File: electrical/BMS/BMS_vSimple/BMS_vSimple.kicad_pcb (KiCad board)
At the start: 2 copper layers, 127 parts, among them J1 Conn_01x04_Pin, J2 Conn_02x12_Top_Bottom, J3 Conn_01x13_Socket, Q6 BCP56, U1 STM32F412RGTx, U2 BQ79652PAPRQ1, U3 ISO1044BD, U4 CD74HC4067M

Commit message: updated pcb
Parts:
- added C39: 100n, Capacitor_SMD:C_0603_1608Metric, F.Cu at (122.4, 81.5)
- added C40: 100n, Capacitor_SMD:C_0603_1608Metric, F.Cu at (130.7, 81.5)
- added C41: 100n, Capacitor_SMD:C_0603_1608Metric, F.Cu at (134.8, 68.7)
- added C42: 100n, Capacitor_SMD:C_0603_1608Metric, F.Cu at (122.6, 64.3)
- added C43: 100n, Capacitor_SMD:C_0603_1608Metric, F.Cu at (118.0, 73.9)
- added H1: MountingHole, MountingHole:MountingHole_2.2mm_M2, F.Cu at (34.0, 65.8)
- added H2: MountingHole, MountingHole:MountingHole_2.2mm_M2, F.Cu at (95.5, 65.5)
- added H3: MountingHole, MountingHole:MountingHole_2.2mm_M2, F.Cu at (154.0, 64.5)
- added H4: MountingHole, MountingHole:MountingHole_2.2mm_M2, F.Cu at (33.0, 139.0)
- added H5: MountingHole, MountingHole:MountingHole_2.2mm_M2, F.Cu at (96.5, 139.2)
- added H6: MountingHole, MountingHole:MountingHole_2.2mm_M2, F.Cu at (154.5, 140.0)
- added TP23: TestPoint, TestPoint:TestPoint_Pad_2.0x2.0mm, F.Cu at (135.1, 80.2)
- added TP24: TestPoint, TestPoint:TestPoint_Pad_2.0x2.0mm, F.Cu at (139.1, 80.2)
- moved C1 119.5 mm to (113.7, 112.1), turned to 90 degrees
- moved C37 110.2 mm to (140.5, 90.6), turned to -90 degrees
- moved R38 109.0 mm to (121.9, 121.0)
- moved R5 108.9 mm to (99.0, 118.8), turned to -90 degrees
- moved R39 104.0 mm to (121.1, 117.7), turned to 90 degrees
- moved C5 103.7 mm to (96.5, 116.0)
- moved R40 103.3 mm to (122.9, 117.6), turned to 90 degrees
- moved C32 102.1 mm to (113.6, 103.2), turned to -90 degrees
- moved C36 101.6 mm to (130.0, 89.8), turned to -90 degrees
- moved R20 100.6 mm to (89.7, 118.8), turned to -90 degrees
- moved C30 99.5 mm to (112.8, 95.3)
- moved C19 99.3 mm to (93.3, 116.0)
- moved C33 99.1 mm to (115.8, 98.8), turned to 90 degrees
- moved R10 95.0 mm to (92.7, 118.8), turned to -90 degrees
- moved R9 94.2 mm to (86.5, 118.8), turned to -90 degrees
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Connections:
- TP7 pad 1: Net-(U1-PA0) -> Net-(U1-PA14)
- U1 pad 1: unconnected-(U1-VBAT-Pad1) -> /VDD1
- U1 pad 13: unconnected-(U1-VDDA-Pad13) -> /VDD1
- U1 pad 14: Net-(U1-PA0) -> unconnected-(U1-PA0-Pad14)
- U1 pad 32: unconnected-(U1-VDD-Pad32) -> /VDD1
- U1 pad 33: unconnected-(U1-PB12-Pad33) -> Net-(U1-PB12)
- U1 pad 37: unconnected-(U1-PC6-Pad37) -> Net-(U1-PC6)
- U1 pad 48: unconnected-(U1-VDD-Pad48) -> /VDD1
- U1 pad 49: unconnected-(U1-PA14-Pad49) -> Net-(U1-PA14)
- U1 pad 64: unconnected-(U1-VDD-Pad64) -> /VDD1
- U3 pad 5: Net-(J1-Pin_2) -> Net-(J1-Pin_1)
- U3 pad 6: Net-(J1-Pin_3) -> Net-(J1-Pin_2)
- U3 pad 7: Net-(J1-Pin_1) -> Net-(J1-Pin_3)
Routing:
- net /BAT+: track 0.00 -> 170.0 mm
- net Net-(C29-Pad1): track 0.00 -> 154.3 mm, vias 0 -> 2
- net /TSREF: track 0.00 -> 120.1 mm, vias 0 -> 14
- net /AVDD: track 0.00 -> 108.9 mm, vias 0 -> 2
- net /VDD1: track 0.00 -> 91.7 mm
- net /CB12: track 0.00 -> 72.1 mm
- net /GPIO2: track 0.00 -> 69.5 mm, vias 0 -> 2
- net /GPIO1: track 0.00 -> 69.4 mm, vias 0 -> 2
- net /GPIO3: track 0.00 -> 69.0 mm, vias 0 -> 2
- net /VC11: track 0.00 -> 68.2 mm, vias 0 -> 3
- net /VC12: track 0.00 -> 67.3 mm, vias 0 -> 2
- net /CB11: track 0.00 -> 64.6 mm
- net /VC10: track 0.00 -> 61.9 mm, vias 0 -> 3
- net /CB10: track 0.00 -> 57.8 mm
- net /VC9: track 0.00 -> 56.9 mm, vias 0 -> 3
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- added copper zone on F.Cu, net /BAT+
- added copper zone on B.Cu, net GND
- added copper zone on F.Cu, net GND
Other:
- board outline added: 133.5 x 84.2 mm

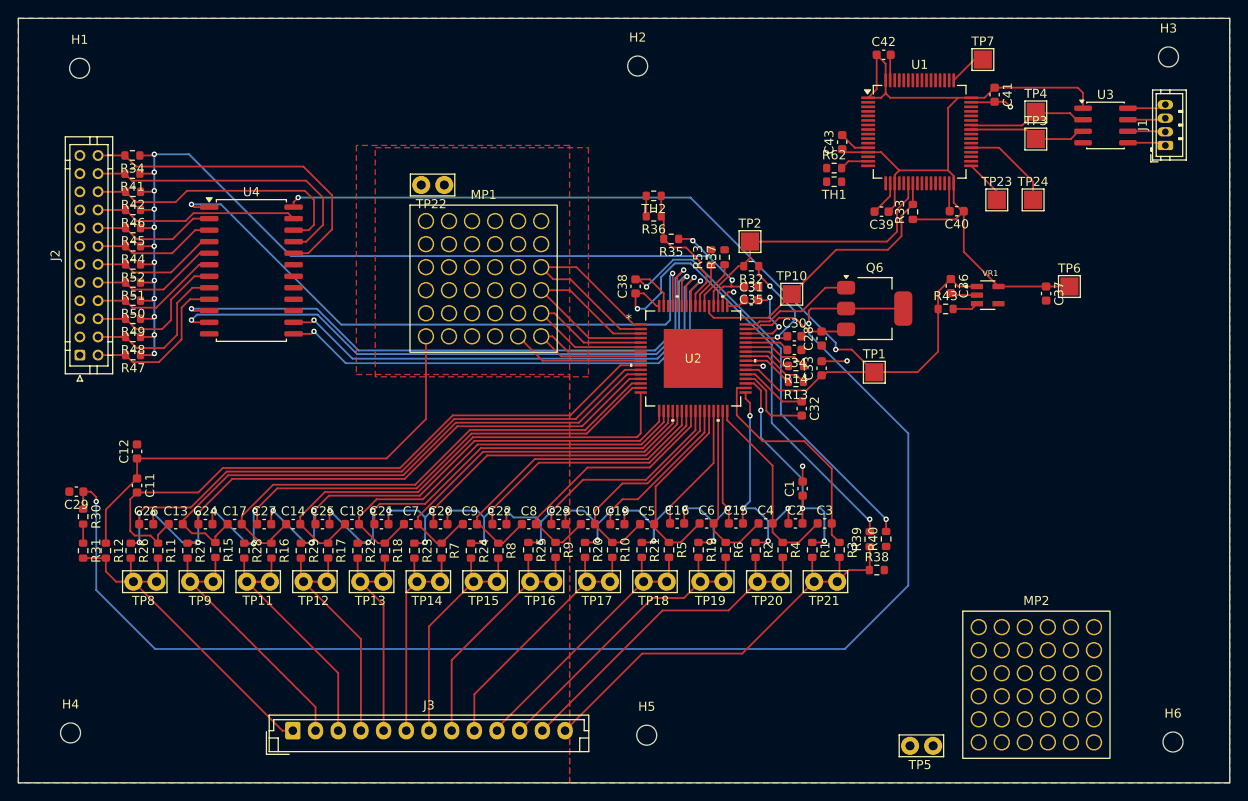
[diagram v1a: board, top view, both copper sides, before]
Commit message: adding mounting holes and finalizing dimensions
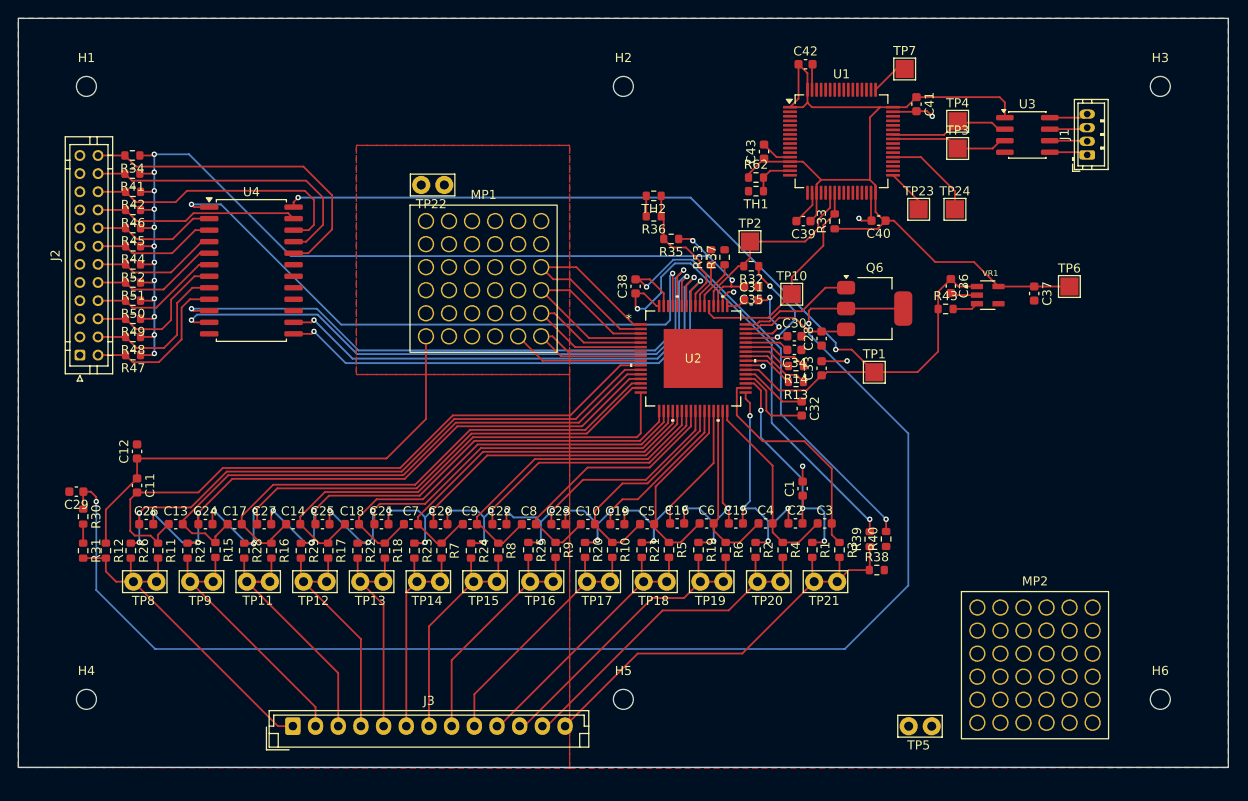
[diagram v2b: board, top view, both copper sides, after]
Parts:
- moved TP24 8.68 mm to (130.5, 81.3)
- moved C41 8.68 mm to (126.2, 69.7)
- moved C43 8.68 mm to (109.4, 74.9)
- moved R62 8.68 mm to (108.5, 77.8)
- moved TH1 8.68 mm to (108.5, 79.3)
- moved TP23 8.68 mm to (126.5, 81.3)
- moved J1 8.68 mm to (145.0, 75.3)
- moved TP7 8.68 mm to (124.9, 65.8)
- moved C39 8.68 mm to (113.8, 82.6)
- moved C40 8.68 mm to (122.1, 82.5)
- moved C42 8.68 mm to (114.0, 65.3)
- moved R33 8.68 mm to (117.2, 82.6)
- moved TP3 8.68 mm to (130.8, 74.6)
- moved TP4 8.68 mm to (130.8, 71.6)
- moved U1 8.68 mm to (118.0, 73.8)
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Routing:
- net /AFE_RX: track 31.6 -> 21.7 mm
- net /VDD1: track 91.7 -> 100.1 mm
- net /AFE_TX: track 32.6 -> 24.7 mm
- net GND: track 50.3 -> 51.8 mm, vias 7 -> 8
- net /PA1: track 3.24 -> 4.74 mm
- net /CELL_9+: track 27.0 -> 26.5 mm
- net /CELL_8+: track 25.4 -> 24.9 mm
- net /CELL_6+: track 26.4 -> 25.9 mm
- net /CELL_5+: track 28.1 -> 27.6 mm
- net /CELL_12+: track 39.8 -> 40.3 mm
- net /CELL_11+: track 30.2 -> 29.7 mm
- net /CELL_10+: track 30.5 -> 30.0 mm
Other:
- board size 133.5 x 84.2 mm -> 133.3 x 82.6 mm

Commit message: bms is smaller now...
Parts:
- added C44: 100n, Capacitor_SMD:C_0603_1608Metric, F.Cu at (127.3, 75.8)
- added C45: 4.7u, Capacitor_SMD:C_0603_1608Metric, F.Cu at (117.8, 86.8)
- added R54: 10k, Resistor_SMD:R_0603_1608Metric, F.Cu at (129.7, 76.5)
- added TP25: TestPoint, TestPoint:TestPoint_Pad_2.0x2.0mm, F.Cu at (136.8, 93.2)
- added TP26: TestPoint, TestPoint:TestPoint_Pad_2.0x2.0mm, F.Cu at (135.2, 82.2)
- J1: footprint Connector_JST:JST_ZH_B4B-ZR_1x04_P1.50mm_Vertical -> Connector_JST:JST_XH_B4B-XH-A_1x04_P2.50mm_Vertical
- J2: value Conn_02x12_Top_Bottom -> Conn_01x12; footprint Connector_JST:JST_PHD_B24B-PHDSS_2x12_P2.00mm_Vertical -> Connector_JST:JST_XH_B12B-XH-A_1x12_P2.50mm_Vertical
- J3: footprint Connector_JST:JST_EH_B13B-EH-A_1x13_P2.50mm_Vertical -> Connector_JST:JST_XH_B13B-XH-A_1x13_P2.50mm_Vertical
- moved MP2 84.3 mm to (66.5, 89.0)
- moved TP5 81.3 mm to (70.2, 78.5)
- moved H6 43.6 mm to (112.1, 120.5)
- moved H3 42.5 mm to (111.7, 77.3)
- moved J1 37.6 mm to (129.0, 109.2), turned to 0 degrees
- moved U3 25.9 mm to (133.5, 98.5), turned to -90 degrees
- moved TP7 24.7 mm to (135.2, 88.2)
- moved J3 23.9 mm to (73.0, 120.0)
- moved C42 23.2 mm to (132.8, 79.0)
- moved TP4 21.9 mm to (133.8, 93.2), turned to -90 degrees
- moved C41 21.1 mm to (131.8, 90.1), turned to 180 degrees
- moved TP3 18.7 mm to (130.8, 93.2), turned to -90 degrees
- moved R31 16.9 mm to (48.8, 110.1)
- moved TP6 16.6 mm to (127.3, 94.8), turned to 90 degrees
- moved R30 16.6 mm to (48.8, 107.1)
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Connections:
- J2 pad 1: GND -> Net-(J2-Pin_1)
- J2 pad 11: GND -> Net-(J2-Pin_11)
- J2 pad 3: GND -> Net-(J2-Pin_3)
- J2 pad 5: GND -> Net-(J2-Pin_5)
- J2 pad 7: GND -> Net-(J2-Pin_7)
- J2 pad 9: GND -> Net-(J2-Pin_9)
- R34 pad 2: Net-(J2-Pin_24) -> Net-(J2-Pin_12)
- R41 pad 2: Net-(J2-Pin_22) -> Net-(J2-Pin_11)
- R42 pad 2: Net-(J2-Pin_20) -> Net-(J2-Pin_10)
- R44 pad 2: Net-(J2-Pin_14) -> Net-(J2-Pin_7)
- R45 pad 2: Net-(J2-Pin_16) -> Net-(J2-Pin_8)
- R46 pad 2: Net-(J2-Pin_18) -> Net-(J2-Pin_9)
- R47 pad 2: Net-(J2-Pin_2) -> Net-(J2-Pin_1)
- R48 pad 2: Net-(J2-Pin_4) -> Net-(J2-Pin_2)
- R49 pad 2: Net-(J2-Pin_6) -> Net-(J2-Pin_3)
- R50 pad 2: Net-(J2-Pin_8) -> Net-(J2-Pin_4)
- R51 pad 2: Net-(J2-Pin_10) -> Net-(J2-Pin_5)
- R52 pad 2: Net-(J2-Pin_12) -> Net-(J2-Pin_6)
- TP24 pad 1: Net-(U1-PC6) -> Net-(U1-PC10)
- U1 pad 30: unconnected-(U1-VCAP_1-Pad30) -> Net-(U1-VCAP_1)
- U1 pad 37: Net-(U1-PC6) -> unconnected-(U1-PC6-Pad37)
- U1 pad 46: unconnected-(U1-PA13-Pad46) -> Net-(U1-PA13)
- U1 pad 51: unconnected-(U1-PC10-Pad51) -> Net-(U1-PC10)
- U1 pad 60: unconnected-(U1-BOOT0-Pad60) -> Net-(U1-BOOT0)
- U1 pad 7: unconnected-(U1-NRST-Pad7) -> Net-(U1-NRST)
- U4 pad 2: Net-(J2-Pin_16) -> Net-(J2-Pin_8)
- U4 pad 20: Net-(J2-Pin_24) -> Net-(J2-Pin_12)
- U4 pad 21: Net-(J2-Pin_22) -> Net-(J2-Pin_11)
- U4 pad 22: Net-(J2-Pin_20) -> Net-(J2-Pin_10)
- U4 pad 23: Net-(J2-Pin_18) -> Net-(J2-Pin_9)
- U4 pad 3: Net-(J2-Pin_14) -> Net-(J2-Pin_7)
- U4 pad 4: Net-(J2-Pin_12) -> Net-(J2-Pin_6)
- U4 pad 5: Net-(J2-Pin_10) -> Net-(J2-Pin_5)
- U4 pad 6: Net-(J2-Pin_8) -> Net-(J2-Pin_4)
- U4 pad 7: Net-(J2-Pin_6) -> Net-(J2-Pin_3)
- U4 pad 8: Net-(J2-Pin_4) -> Net-(J2-Pin_2)
- U4 pad 9: Net-(J2-Pin_2) -> Net-(J2-Pin_1)
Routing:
- net /BAT+: track 170.0 -> 96.6 mm
- net GND: track 51.8 -> 102.7 mm, vias 8 -> 7
- net Net-(J2-Pin_24): track 36.7 -> 0.00 mm
- net Net-(C29-Pad1): track 154.3 -> 119.6 mm
- net Net-(J2-Pin_22): track 32.9 -> 0.00 mm
- net Net-(J2-Pin_20): track 30.4 -> 0.00 mm
- net Net-(J2-Pin_11): track 0.00 -> 30.2 mm
- net Net-(J2-Pin_18): track 22.7 -> 0.00 mm
- net Net-(J2-Pin_9): track 0.00 -> 20.8 mm
- net Net-(J2-Pin_1): track 0.00 -> 20.7 mm
- net /CB12: track 72.1 -> 51.5 mm
- net Net-(J2-Pin_12): track 14.0 -> 33.2 mm
- net /VC9: track 56.9 -> 39.5 mm, vias 3 -> 4
- net /VC8: track 51.6 -> 34.5 mm, vias 3 -> 4
- net /VC12: track 67.3 -> 50.9 mm
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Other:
- board size 133.3 x 82.6 mm -> 109 x 52.9 mm

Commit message: bms pcb layout v2
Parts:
- moved H5 71.6 mm to (56.6, 67.9)
- moved H2 38.7 mm to (56.6, 77.9)
- moved H4 23.3 mm to (56.5, 120.8)
- moved H3 3.95 mm to (115.6, 77.9)
- moved H6 3.55 mm to (115.6, 120.8)
- moved C39 1.59 mm to (117.6, 81.4), turned to 180 degrees
- moved R33 0.33 mm to (117.0, 83.7)
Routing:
- net /VDD1: track 95.5 -> 93.2 mm
- added copper zone on In1.Cu, net GND
- added copper zone on In2.Cu, net GND
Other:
- copper layers 2 -> 4
